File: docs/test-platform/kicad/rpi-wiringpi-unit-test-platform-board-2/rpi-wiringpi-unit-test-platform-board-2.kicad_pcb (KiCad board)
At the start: 2 copper layers, 92.7 x 67.3 mm, 23 parts, among them J1 IN_PWR, J2 IN_SIGNAL, J3 IN_CS_SHIFTREG, J5 OUT_SERVO, SW1 SW_BOARD_CONN_LED, U1 MCP3008, U2 MCP4922, U3 MCP42010, U4 ADS1115, U5 74HC595

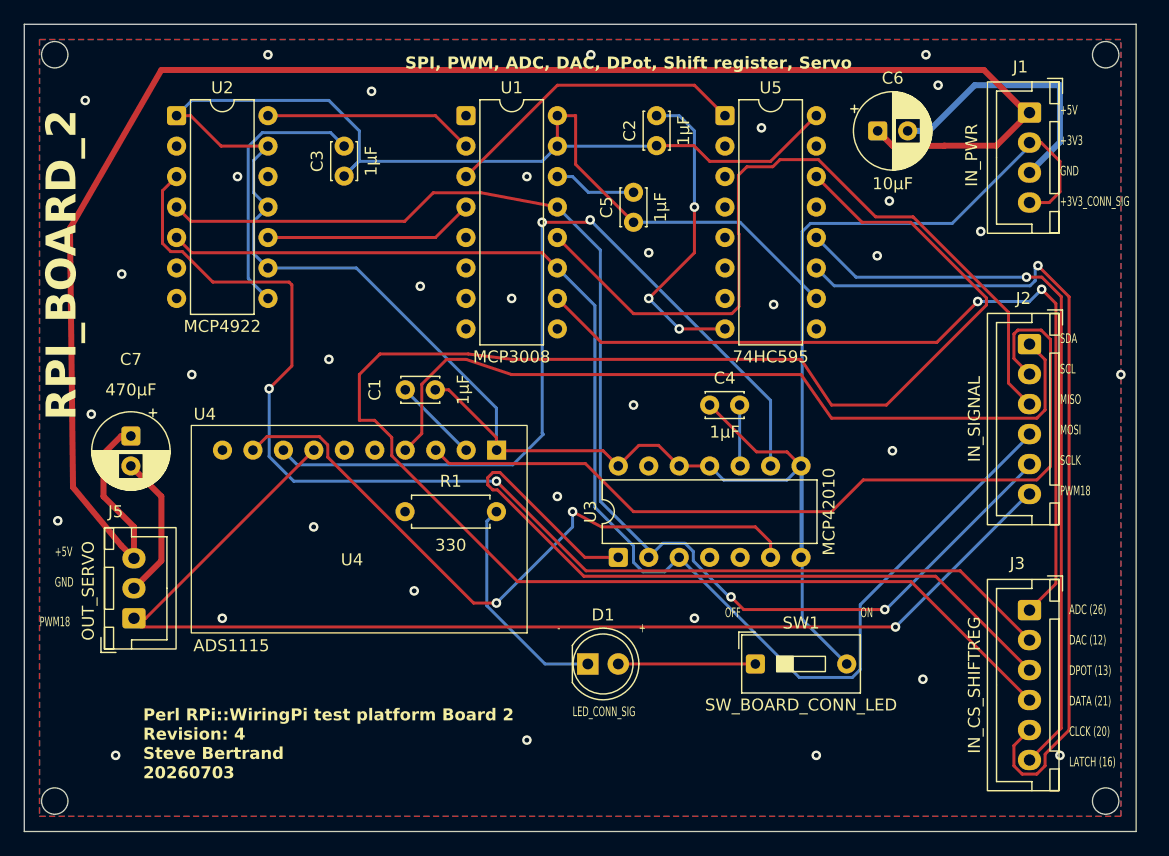
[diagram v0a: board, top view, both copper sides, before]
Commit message: Add proper caps; clean up tracing, update mislabeled caps
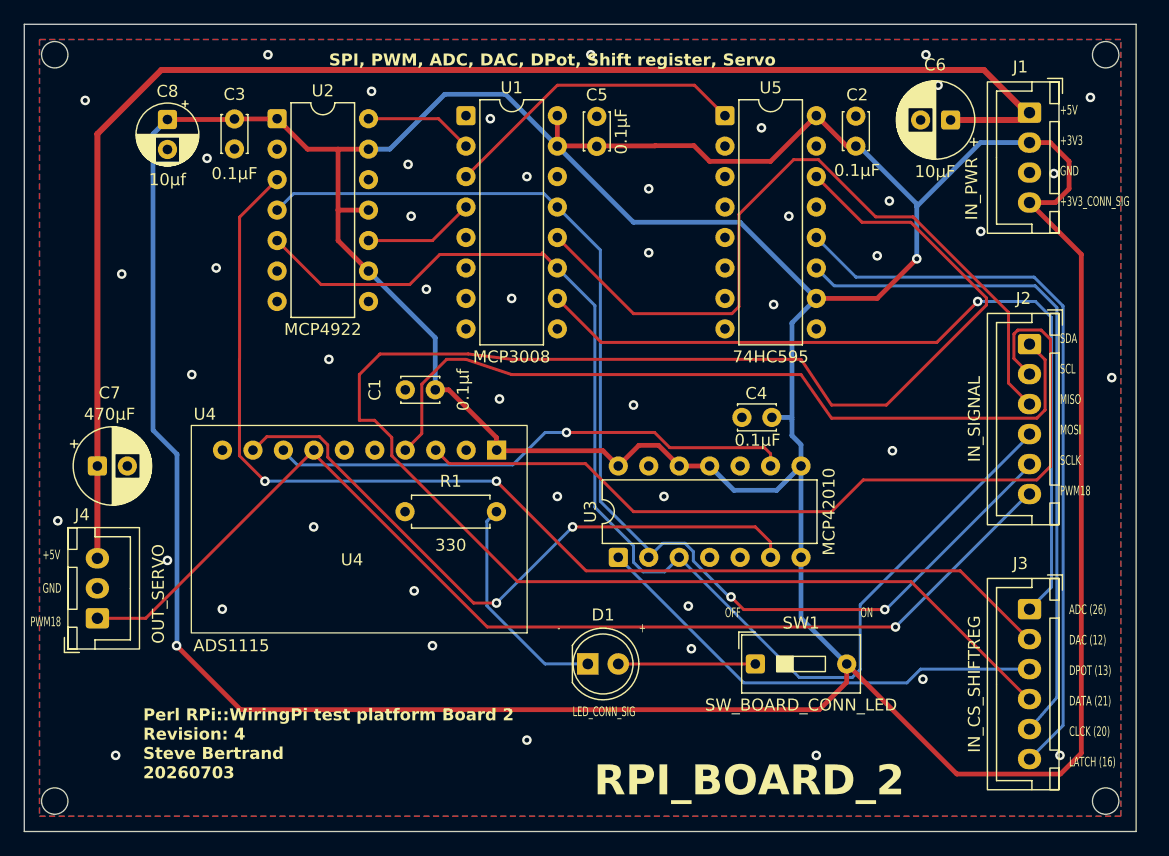
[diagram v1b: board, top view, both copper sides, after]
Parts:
- added C8: 10µf, Capacitor_THT:CP_Radial_D5.0mm_P2.50mm, F.Cu at (161.8, 53.7)
- C1: value 1µF -> 0.1µf
- C2, C3, C4, C5: value 1µF -> 0.1µF
- moved C2 16.6 mm to (219.2, 55.9)
- moved C3 10.3 mm to (167.4, 53.6), turned to -90 degrees
- moved U2 8.39 mm to (170.9, 53.6)
- moved C5 7.03 mm to (197.6, 55.9)
- moved C6 6.15 mm to (227.1, 53.7), turned to 180 degrees
- moved C4 5.29 mm to (212.2, 78.5), turned to 180 degrees
- moved C7 3.75 mm to (156.0, 82.5), turned to 0 degrees
- moved J4 3.05 mm to (156.0, 95.2)
- moved J3 0.08 mm to (233.7, 94.5)
- renumbered J5 to J4
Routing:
- net +3V3: track 266.4 -> 413.7 mm, vias 0 -> 2
- net GND: track 102.9 -> 0.08 mm, vias 37 -> 46
- net /DPOT_WIPER_A: track 71.8 -> 44.0 mm, vias 2 -> 1
- net /CS_DPOT: track 66.2 -> 39.1 mm
- net +5V: track 144.9 -> 123.7 mm
- net /SR_CLK: track 70.9 -> 57.4 mm, vias 1 -> 0
- net /SPI_SCLK: track 105.1 -> 96.2 mm
- net /DAC_A_CH1: track 17.6 -> 9.07 mm
- net /DAC_B_CH3: track 17.6 -> 9.29 mm
- net /PWM18: track 102.1 -> 94.5 mm
- net /CS_DAC: track 103.1 -> 96.6 mm
- net /SPI_MOSI: track 109.5 -> 104.9 mm
- net /CS_ADC: track 71.9 -> 69.8 mm, vias 2 -> 1
- net /SPI_MISO: track 65.7 -> 63.7 mm
- net /DPOT_WIPER_B: track 56.0 -> 54.4 mm
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
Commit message: Added JST for future servo position sensors (connected to MCP3008)
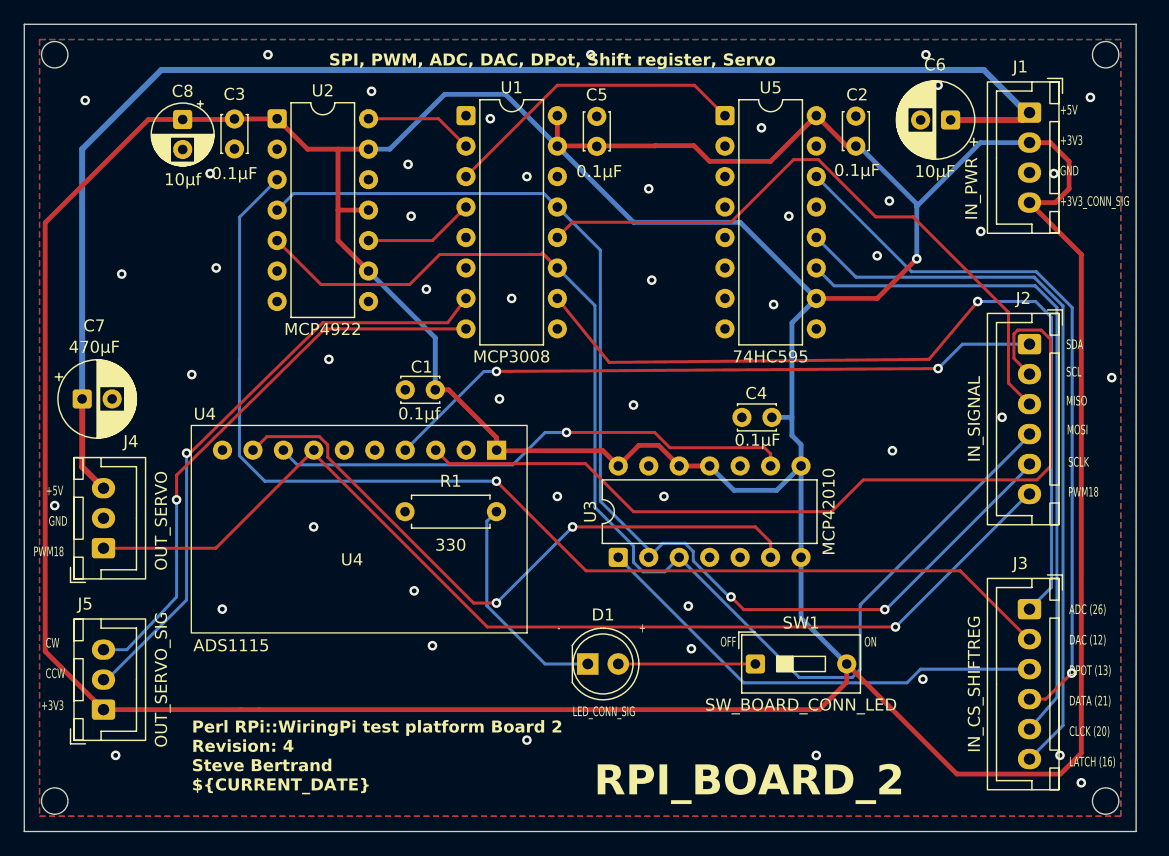
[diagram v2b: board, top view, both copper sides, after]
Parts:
- added J5: OUT_SERVO_SIG, Connector_JST:JST_XH_B3B-XH-A_1x03_P2.50mm_Vertical, F.Cu at (156.5, 102.9)
- moved J4 5.86 mm to (156.5, 89.4)
- moved C7 5.73 mm to (154.7, 77.0)
- moved C8 1.27 mm to (163.1, 53.7)
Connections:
- U1 pad 7: unconnected-(U1-CH6-Pad7) -> /CCW
- U1 pad 8: unconnected-(U1-CH7-Pad8) -> /CW
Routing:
- net /SR_DATA: track 147.7 -> 60.8 mm, vias 0 -> 1
- net /CCW: track 0.00 -> 50.7 mm, vias 0 -> 1
- net /CW: track 0.00 -> 47.3 mm, vias 0 -> 1
- net +3V3: track 413.7 -> 430.0 mm, vias 2 -> 1
- net /I2C_SDA: track 67.3 -> 55.6 mm, vias 0 -> 2
- net /SPI_MISO: track 63.7 -> 54.0 mm
- net +5V: track 123.7 -> 119.2 mm
- net /PWM18: track 94.5 -> 91.6 mm
- net /CS_ADC: track 69.8 -> 71.6 mm
- net GND: vias 46 -> 47
- net /CS_DAC: vias 2 -> 1
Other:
- board text added: "CCW"
- board text added: "CW"
- board text added: "Perl RPi::WiringPi test platform Board 2 Revision: ${REVISION} Steve Bertrand ${CURRENT_DATE}"
- board text removed: "Perl RPi::WiringPi test platform Board 2 Revision: ${REVISION} Steve Bertrand 20260703"

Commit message: Tweaks and cleanup
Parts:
- added C9: 0.1µf, Capacitor_THT:C_Disc_D3.0mm_W2.0mm_P2.50mm, F.Cu at (156.5, 79.8)
- moved C7 2.80 mm to (156.5, 74.8)
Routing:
- net /DPOT_WIPER_B: track 54.4 -> 50.6 mm
- net /PWM18: track 91.6 -> 88.6 mm
- net +5V: track 119.2 -> 117.7 mm
- net /SPI_SCLK: track 96.2 -> 95.2 mm

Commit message: Fix capacitor conflicts related to datasheets; add cap conflict checks to build
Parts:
- C1: value 0.1µf -> 0.1µF
- C5: value 0.1µF -> 1µf
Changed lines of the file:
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@@
 	(title_block
 		(date "2026-07-22")
-		(rev "4")
+		(rev "5")
 	)
 	(layers
@@
 			)
 		)
-		(property "Value" "0.1µf"
+		(property "Value" "0.1µF"
 			(at 1.33 -2 180)
 			(layer "F.SilkS")
@@
 			)
 		)
-		(property "Value" "0.1µF"
+		(property "Value" "1µf"
 			(at -2.1 0.2 180)
 			(layer "F.SilkS")
@@
 	)
 	(segment
+		(start 186.69 68.58)
+		(end 185.166 70.612)
+		(width 0.25)
+		(layer "F.Cu")
+		(net "/CCW")
+	)
+	(segment
+		(start 163.679755 81.478946)
+		(end 163.39257 81.478946)
+		(width 0.25)
+		(layer "F.Cu")
+		(net "/CCW")
+	)
+	(segment
+		(start 185.166 70.612)
+		(end 174.752 70.612)
+		(width 0.25)
+		(layer "F.Cu")
+		(net "/CCW")
+	)
+	(segment
+		(start 174.752 70.612)
+		(end 163.679755 81.478946)
+		(width 0.25)
+		(layer "F.Cu")
+		(net "/CCW")
+	)
+	(via
+		(at 163.39257 81.478946)
+		(size 0.8)
+		(drill 0.4)
+		(layers "F.Cu" "B.Cu")
+		(net "/CCW")
+	)
+	(segment
+		(start 156.74857 100.37)
+		(end 163.39257 93.726)
+		(width 0.25)
+		(layer "B.Cu")
+		(net "/CCW")
+	)
+	(segment
+		(start 163.39257 93.726)
+		(end 163.39257 81.478946)
+		(width 0.25)
+		(layer "B.Cu")
+		(net "/CCW")
+	)
+	(segment
+		(start 156.464 100.37)
+		(end 156.74857 100.37)
+		(width 0.25)
+		(layer "B.Cu")
+		(net "/CCW")
+	)
+	(segment
+		(start 162.56 83.321034)
+		(end 162.564517 83.316517)
+		(width 0.25)
+		(layer "F.Cu")
+		(net "/CW")
+	)
+	(segment
+		(start 162.564517 83.316517)
+		(end 174.906509 71.12)
+		(width 0.25)
+		(layer "F.Cu")
+		(net "/CW")
+	)
+	(segment
+		(start 162.56 85.373003)
+		(end 162.56 83.321034)
+		(width 0.25)
+		(layer "F.Cu")
+		(net "/CW")
+	)
+	(segment
+		(start 174.906509 71.12)
+		(end 186.69 71.12)
+		(width 0.25)
+		(layer "F.Cu")
+		(net "/CW")
+	)
+	(via
+		(at 162.56 85.373003)
+		(size 0.8)
+		(drill 0.4)
+		(layers "F.Cu" "B.Cu")
+		(net "/CW")
+	)
+	(segment
+		(start 162.56 93.472)
+		(end 158.416 97.87)
+		(width 0.25)
+		(layer "B.Cu")
+		(net "/CW")
+	)
+	(segment
+		(start 162.56 85.373003)
+		(end 162.56 93.472)
+		(width 0.25)
+		(layer "B.Cu")
+		(net "/CW")
+	)
+	(segment
+		(start 158.416 97.87)
+		(end 156.464 97.87)
+		(width 0.25)
+		(layer "B.Cu")
+		(net "/CW")
+	)
+	(segment
 		(start 223.459695 100.635)
 		(end 224.606695 99.488)
@@
 		(net "/I2C_SDA")
 	)
-	(segment
-		(start 186.69 68.58)
-		(end 185.166 70.612)
-		(width 0.25)
-		(layer "F.Cu")
-		(net "/CCW")
-	)
-	(segment
-		(start 163.679755 81.478946)
-		(end 163.39257 81.478946)
-		(width 0.25)
-		(layer "F.Cu")
-		(net "/CCW")
-	)
-	(segment
-		(start 185.166 70.612)
-		(end 174.752 70.612)
-		(width 0.25)
-		(layer "F.Cu")
-		(net "/CCW")
-	)
-	(segment
-		(start 174.752 70.612)
-		(end 163.679755 81.478946)
-		(width 0.25)
-		(layer "F.Cu")
-		(net "/CCW")
-	)
-	(via
-		(at 163.39257 81.478946)
-		(size 0.8)
-		(drill 0.4)
-		(layers "F.Cu" "B.Cu")
-		(net "/CCW")
-	)
-	(segment
-		(start 156.74857 100.37)
-		(end 163.39257 93.726)
-		(width 0.25)
-		(layer "B.Cu")
-		(net "/CCW")
-	)
-	(segment
-		(start 163.39257 93.726)
-		(end 163.39257 81.478946)
-		(width 0.25)
-		(layer "B.Cu")
-		(net "/CCW")
-	)
-	(segment
-		(start 156.464 100.37)
-		(end 156.74857 100.37)
-		(width 0.25)
-		(layer "B.Cu")
-		(net "/CCW")
-	)
-	(segment
-		(start 162.56 83.321034)
-		(end 162.564517 83.316517)
-		(width 0.25)
-		(layer "F.Cu")
-		(net "/CW")
-	)
-	(segment
-		(start 162.564517 83.316517)
-		(end 174.906509 71.12)
-		(width 0.25)
-		(layer "F.Cu")
-		(net "/CW")
-	)
-	(segment
-		(start 162.56 85.373003)
-		(end 162.56 83.321034)
-		(width 0.25)
-		(layer "F.Cu")
-		(net "/CW")
-	)
-	(segment
-		(start 174.906509 71.12)
-		(end 186.69 71.12)
-		(width 0.25)
-		(layer "F.Cu")
-		(net "/CW")
-	)
-	(via
-		(at 162.56 85.373003)
-		(size 0.8)
-		(drill 0.4)
-		(layers "F.Cu" "B.Cu")
-		(net "/CW")
-	)
-	(segment
-		(start 162.56 93.472)
-		(end 158.416 97.87)
-		(width 0.25)
-		(layer "B.Cu")
-		(net "/CW")
-	)
-	(segment
-		(start 162.56 85.373003)
-		(end 162.56 93.472)
-		(width 0.25)
-		(layer "B.Cu")
-		(net "/CW")
-	)
-	(segment
-		(start 158.416 97.87)
-		(end 156.464 97.87)
-		(width 0.25)
-		(layer "B.Cu")
-		(net "/CW")
-	)
 	(zone

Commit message: Change footprint of cap to tantalum for the mcp4922
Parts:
- C8: footprint Capacitor_THT:CP_Radial_D5.0mm_P2.50mm -> Capacitor_THT:CP_Radial_Tantal_D5.0mm_P2.50mm

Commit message: Re-footprint caps
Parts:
- C6: footprint Capacitor_THT:CP_Radial_D6.3mm_P2.50mm -> Capacitor_THT:CP_Radial_D5.0mm_P2.50mm
- C7: footprint Capacitor_THT:CP_Radial_D6.3mm_P2.50mm -> Capacitor_THT:CP_Radial_D8.0mm_P2.50mm
- moved C7 0.63 mm to (156.5, 74.2)

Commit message: Cleanup tracing
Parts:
- D1: value LED_BOARD_CONN -> LED_BRD_CONN_SIG
- SW1: value SW_BOARD_CONN_LED -> SW_BRD_CONN_SIG
- moved C1 5.26 mm to (189.2, 77.5), turned to 0 degrees
- moved C5 2.54 mm to (197.6, 53.4), turned to -90 degrees
- moved C4 2.42 mm to (214.6, 78.7)
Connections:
- J1 pad 4: +3V3 -> /CONN_SIG
- SW1 pad 2: +3V3 -> /CONN_SIG
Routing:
- net /CONN_SIG: track 0.00 -> 72.5 mm
- net +3V3: track 430.0 -> 396.0 mm, vias 1 -> 3
- net /SPI_MOSI: track 104.9 -> 103.1 mm
- net /I2C_SDA: vias 2 -> 1
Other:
- board text added: "BRD_CONN_SIG"
- board text added: "LED_BRD_CONN_SIG"
- board text removed: "+3V3_CONN_SIG"
- board text removed: "LED_CONN_SIG"

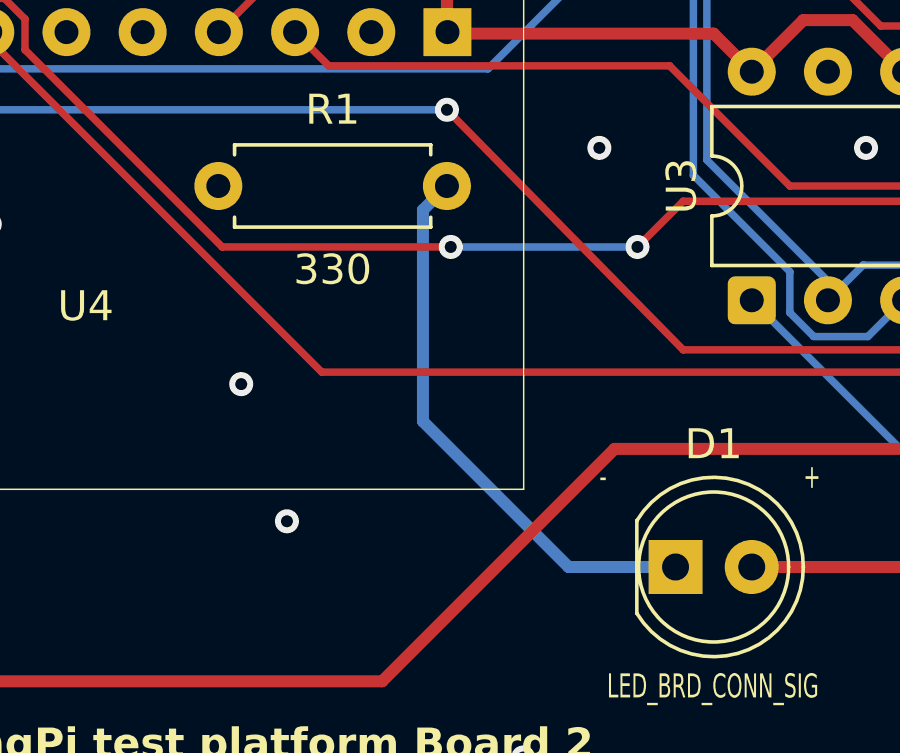
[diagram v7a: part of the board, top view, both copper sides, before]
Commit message: Added script to collect info from kicad
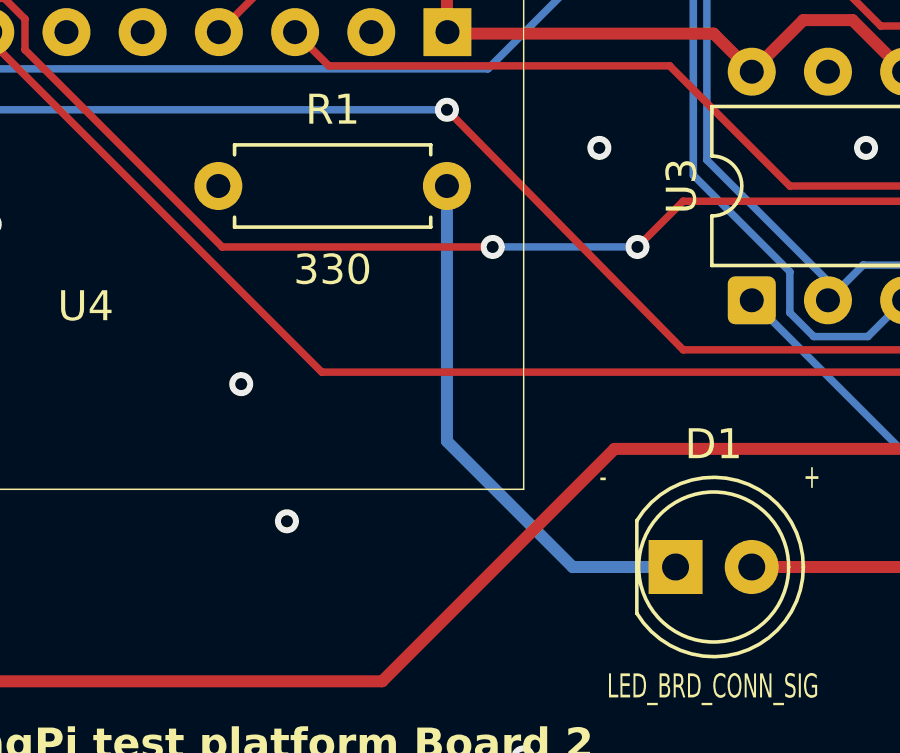
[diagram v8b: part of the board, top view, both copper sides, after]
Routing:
- net Net-(D1-K): track 18.6 -> 17.9 mm
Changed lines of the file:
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@@
-	)
-	(segment
-		(start 189.357 88.392)
-		(end 181.738396 88.392)
-		(width 0.25)
-		(layer "F.Cu")
-		(net "/DPOT_WIPER_B")
 	)
 	(segment
@@
 	)
 	(segment
+		(start 170.085 80.105)
+		(end 168.91 81.28)
+		(width 0.25)
+		(layer "F.Cu")
+		(net "/DPOT_WIPER_B")
+	)
+	(segment
+		(start 181.738396 88.392)
+		(end 175.165 81.818604)
+		(width 0.25)
+		(layer "F.Cu")
+		(net "/DPOT_WIPER_B")
+	)
+	(segment
 		(start 197.104 86.868)
 		(end 210.439 86.868)
@@
 	)
 	(segment
+		(start 190.754 88.392)
+		(end 181.738396 88.392)
+		(width 0.25)
+		(layer "F.Cu")
+		(net "/DPOT_WIPER_B")
+	)
+	(segment
+		(start 175.165 80.793299)
+		(end 174.476701 80.105)
+		(width 0.25)
+		(layer "F.Cu")
+		(net "/DPOT_WIPER_B")
+	)
+	(segment
 		(start 210.439 86.868)
 		(end 212.09 88.9)
@@
 	)
 	(segment
-		(start 181.738396 88.392)
-		(end 175.165 81.818604)
+		(start 175.165 81.818604)
+		(end 175.165 80.793299)
 		(width 0.25)
 		(layer "F.Cu")
@@
 		(net "/DPOT_WIPER_B")
 	)
-	(segment
-		(start 170.085 80.105)
-		(end 168.91 81.28)
-		(width 0.25)
-		(layer "F.Cu")
-		(net "/DPOT_WIPER_B")
-	)
-	(segment
-		(start 175.165 81.818604)
-		(end 175.165 80.793299)
-		(width 0.25)
-		(layer "F.Cu")
-		(net "/DPOT_WIPER_B")
-	)
-	(segment
-		(start 175.165 80.793299)
-		(end 174.476701 80.105)
-		(width 0.25)
-		(layer "F.Cu")
-		(net "/DPOT_WIPER_B")
-	)
 	(via
-		(at 189.357 88.392)
+		(at 190.754 88.392)
 		(size 0.8)
 		(drill 0.4)
@@
 	)
 	(segment
-		(start 189.357 88.392)
+		(start 190.754 88.392)
 		(end 195.58 88.392)
 		(width 0.25)
@@
 	)
 	(segment
-		(start 188.430001 87.159999)
-		(end 188.430001 94.205306)
-		(width 0.4)
-		(layer "B.Cu")
-		(net "Net-(D1-K)")
-	)
-	(segment
-		(start 188.430001 94.205306)
-		(end 193.284695 99.06)
-		(width 0.4)
-		(layer "B.Cu")
-		(net "Net-(D1-K)")
-	)
-	(segment
-		(start 189.23 86.36)
-		(end 188.430001 87.159999)
-		(width 0.4)
-		(layer "B.Cu")
-		(net "Net-(D1-K)")
-	)
-	(segment
-		(start 193.284695 99.06)
+		(start 193.421 99.06)
 		(end 196.85 99.06)
 		(width 0.4)
 		(layer "B.Cu")
+		(net "Net-(D1-K)")
+	)
+	(segment
+		(start 189.23 86.36)
+		(end 189.23 94.869)
+		(width 0.4)
+		(layer "B.Cu")
+		(net "Net-(D1-K)")
+	)
+	(segment
+		(start 189.23 94.869)
+		(end 193.421 99.06)
+		(width 0.4)
+		(layer "B.Cu")
